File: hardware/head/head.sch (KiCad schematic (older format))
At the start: 51 parts, among them J1 DB9_Male, J10 Pump_Active, J2 Stats_Button, J3 Flush_Button, J4 Brew_Button, J5 Temp_Ok, J6 Display, J7 Load_Cell, J8 Rotary_Encoder, J9 Heater_Active, Q1 IRF540N, U1 Teensy4.0, U2 MAX757, U3 INA126, U4 INA126, U5 INA126

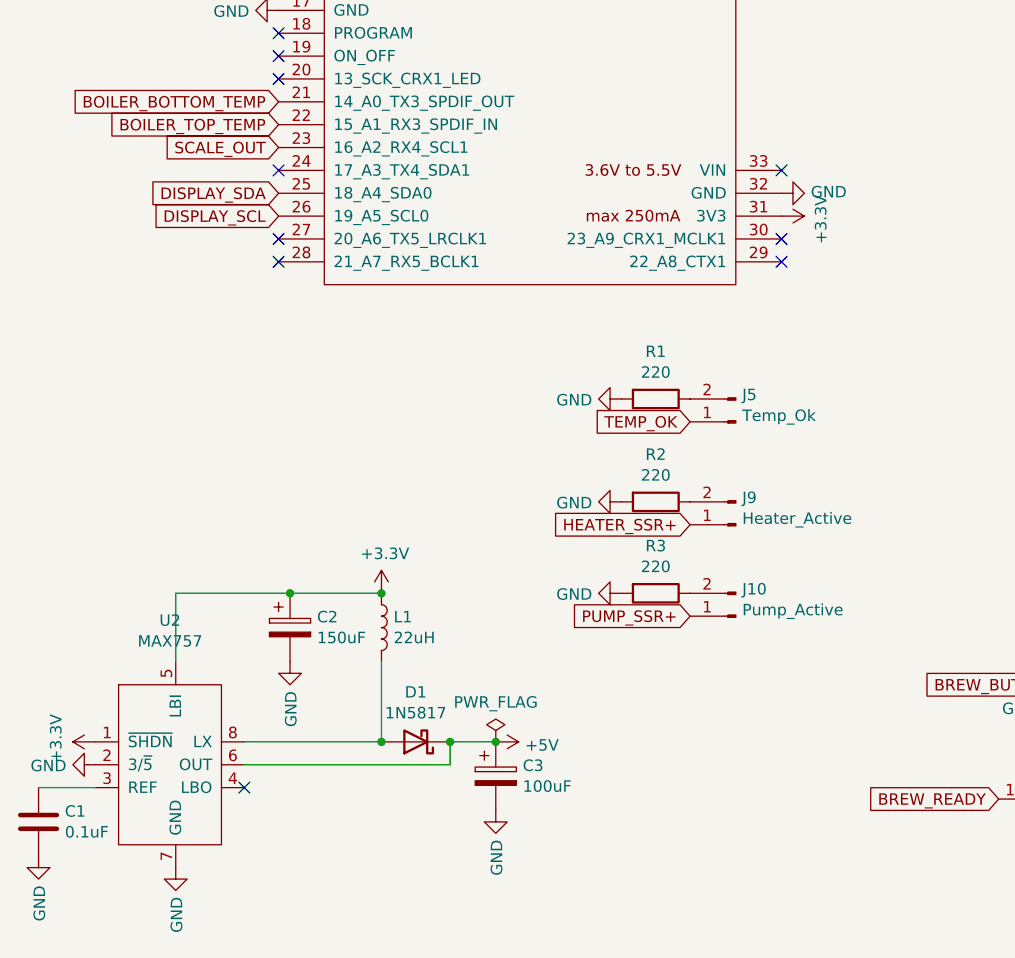
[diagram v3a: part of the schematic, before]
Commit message: Remove unnecessary boost converter
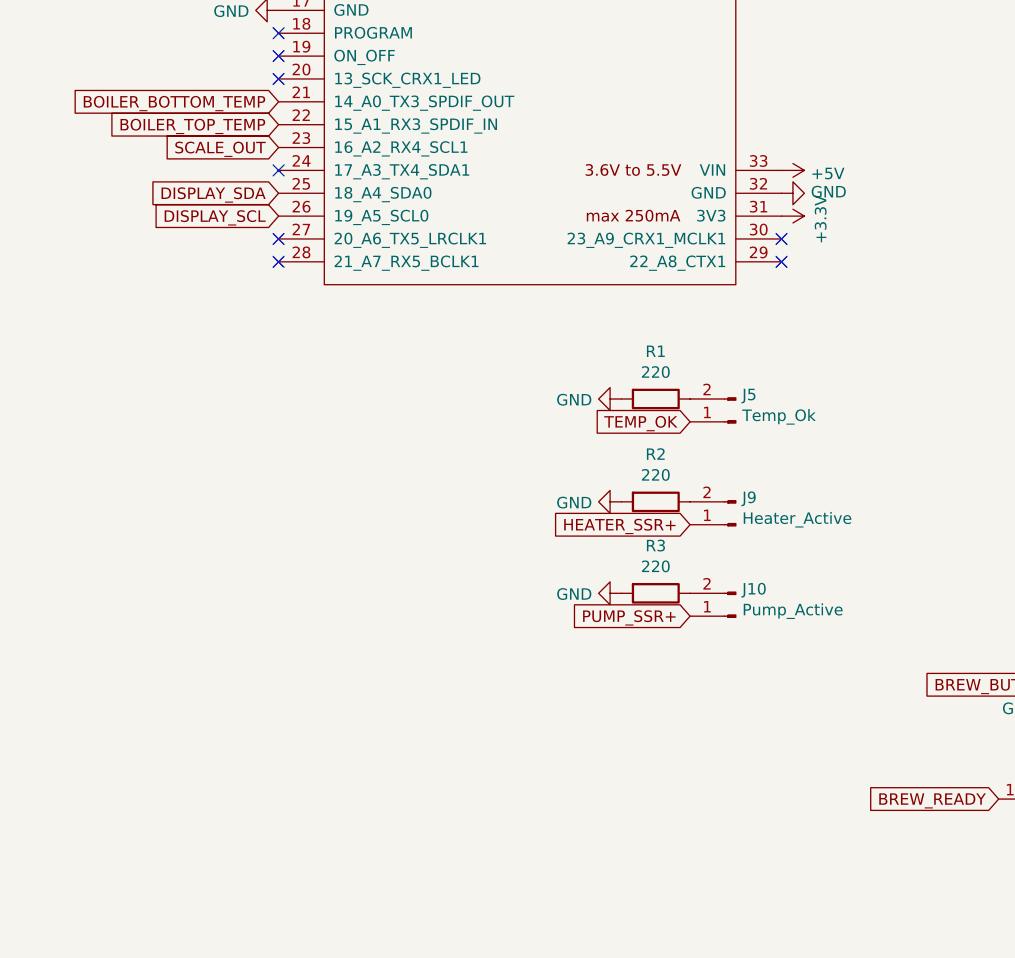
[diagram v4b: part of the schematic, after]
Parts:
- removed C1: 0.1uF, Capacitor_THT:C_Disc_D5.1mm_W3.2mm_P5.00mm, symbol Device:C
- removed C2: 150uF, Capacitor_THT:CP_Radial_D5.0mm_P2.00mm, symbol Device:CP
- removed C3: 100uF, Capacitor_THT:CP_Radial_D5.0mm_P2.00mm, symbol Device:CP
- removed D1: 1N5817, Diode_THT:D_DO-41_SOD81_P10.16mm_Horizontal, symbol Diode:1N5817
- removed L1: 22uH, Inductor_THT:L_Axial_L11.0mm_D4.5mm_P15.24mm_Horizontal_Fastron_MECC, symbol Device:L
- removed U2: MAX757, Package_DIP:DIP-8_W7.62mm, symbol boost_converter:MAX757
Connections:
- net +5V: now also U1.33 (VIN)
- no-connect marks 16 -> 14
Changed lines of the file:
@@
 NoConn ~ 1900 4600
 NoConn ~ 1900 4700
-NoConn ~ 4100 4300
 NoConn ~ 4100 4600
 NoConn ~ 4100 4700
@@
 SCALE_OUT
 $Comp
-L boost_converter:MAX757 U2
-U 1 1 6070BCF1
-P 1450 6900
-F 0 "U2" H 1425 7531 50  0000 C CNN
-F 1 "MAX757" H 1425 7440 50  0000 C CNN
-F 2 "Package_DIP:DIP-8_W7.62mm" H 1450 7600 50  0001 C CNN
-F 3 "" H 1450 7600 50  0001 C CNN
-	1    1450 6900
-	1    0    0    -1
-$EndComp
-$Comp
-L Device:C C1
-U 1 1 6070C612
-P 850 7150
-F 0 "C1" H 965 7196 50  0000 L CNN
-F 1 "0.1uF" H 965 7105 50  0000 L CNN
-F 2 "Capacitor_THT:C_Disc_D5.1mm_W3.2mm_P5.00mm" H 888 7000 50  0001 C CNN
-F 3 "~" H 850 7150 50  0001 C CNN
-	1    850  7150
-	1    0    0    -1
-$EndComp
-$Comp
-L Device:CP C2
-U 1 1 6070D658
-P 1950 6300
-F 0 "C2" H 2068 6346 50  0000 L CNN
-F 1 "150uF" H 2068 6255 50  0000 L CNN
-F 2 "Capacitor_THT:CP_Radial_D5.0mm_P2.00mm" H 1988 6150 50  0001 C CNN
-F 3 "~" H 1950 6300 50  0001 C CNN
-	1    1950 6300
-	1    0    0    -1
-$EndComp
-$Comp
-L Device:CP C3
-U 1 1 6070D8AB
-P 2850 6950
-F 0 "C3" H 2968 6996 50  0000 L CNN
-F 1 "100uF" H 2968 6905 50  0000 L CNN
-F 2 "Capacitor_THT:CP_Radial_D5.0mm_P2.00mm" H 2888 6800 50  0001 C CNN
-F 3 "~" H 2850 6950 50  0001 C CNN
-	1    2850 6950
-	1    0    0    -1
-$EndComp
-$Comp
-L power:GND #PWR010
-U 1 1 6070DB12
-P 1100 6900
-F 0 "#PWR010" H 1100 6650 50  0001 C CNN
-F 1 "GND" V 1105 6772 50  0000 R CNN
-F 2 "" H 1100 6900 50  0001 C CNN
-F 3 "" H 1100 6900 50  0001 C CNN
-	1    1100 6900
-	0    1    1    0
-$EndComp
-$Comp
-L power:+3.3V #PWR09
-U 1 1 6070EA45
-P 1100 6800
-F 0 "#PWR09" H 1100 6650 50  0001 C CNN
-F 1 "+3.3V" H 1115 6973 50  0000 C CNN
-F 2 "" H 1100 6800 50  0001 C CNN
-F 3 "" H 1100 6800 50  0001 C CNN
-	1    1100 6800
-	0    -1   -1   0
-$EndComp
-$Comp
-L power:GND #PWR06
-U 1 1 60710154
-P 850 7300
-F 0 "#PWR06" H 850 7050 50  0001 C CNN
-F 1 "GND" V 855 7172 50  0000 R CNN
-F 2 "" H 850 7300 50  0001 C CNN
-F 3 "" H 850 7300 50  0001 C CNN
-	1    850  7300
-	1    0    0    -1
-$EndComp
-Wire Wire Line
-	850  7000 1100 7000
-NoConn ~ 1750 7000
-$Comp
-L power:+3.3V #PWR013
-U 1 1 607179E9
-P 2350 6150
-F 0 "#PWR013" H 2350 6000 50  0001 C CNN
-F 1 "+3.3V" H 2365 6323 50  0000 C CNN
-F 2 "" H 2350 6150 50  0001 C CNN
-F 3 "" H 2350 6150 50  0001 C CNN
-	1    2350 6150
-	1    0    0    -1
-$EndComp
-$Comp
-L power:GND #PWR011
-U 1 1 6070E0B3
-P 1450 7350
-F 0 "#PWR011" H 1450 7100 50  0001 C CNN
-F 1 "GND" V 1455 7222 50  0000 R CNN
-F 2 "" H 1450 7350 50  0001 C CNN
-F 3 "" H 1450 7350 50  0001 C CNN
-	1    1450 7350
-	1    0    0    -1
-$EndComp
-$Comp
-L power:GND #PWR012
-U 1 1 6071A4A4
-P 1950 6450
-F 0 "#PWR012" H 1950 6200 50  0001 C CNN
-F 1 "GND" V 1955 6322 50  0000 R CNN
-F 2 "" H 1950 6450 50  0001 C CNN
-F 3 "" H 1950 6450 50  0001 C CNN
-	1    1950 6450
-	1    0    0    -1
-$EndComp
-$Comp
-L Device:L L1
-U 1 1 6071AEE1
-P 2350 6300
-F 0 "L1" H 2403 6346 50  0000 L CNN
-F 1 "22uH" H 2403 6255 50  0000 L CNN
-F 2 "Inductor_THT:L_Axial_L11.0mm_D4.5mm_P15.24mm_Horizontal_Fastron_MECC" H 2350 6300 50  0001 C CNN
-F 3 "~" H 2350 6300 50  0001 C CNN
-	1    2350 6300
-	1    0    0    -1
-$EndComp
-Wire Wire Line
-	1450 6450 1450 6150
-Wire Wire Line
-	1450 6150 1950 6150
-Wire Wire Line
-	1950 6150 2350 6150
-Connection ~ 1950 6150
-Connection ~ 2350 6150
-Wire Wire Line
-	1750 6800 2350 6800
-Wire Wire Line
-	2350 6800 2350 6450
-$Comp
-L Diode:1N5817 D1
-U 1 1 60722C26
-P 2500 6800
-F 0 "D1" H 2500 6583 50  0000 C CNN
-F 1 "1N5817" H 2500 6674 50  0000 C CNN
-F 2 "Diode_THT:D_DO-41_SOD81_P10.16mm_Horizontal" H 2500 6625 50  0001 C CNN
-F 3 "http://www.vishay.com/docs/88525/1n5817.pdf" H 2500 6800 50  0001 C CNN
-	1    2500 6800
-	-1   0    0    1
-$EndComp
-Connection ~ 2350 6800
-$Comp
-L power:GND #PWR015
-U 1 1 60724B14
-P 2850 7100
-F 0 "#PWR015" H 2850 6850 50  0001 C CNN
-F 1 "GND" V 2855 6972 50  0000 R CNN
-F 2 "" H 2850 7100 50  0001 C CNN
-F 3 "" H 2850 7100 50  0001 C CNN
-	1    2850 7100
-	1    0    0    -1
-$EndComp
-Wire Wire Line
-	2650 6800 2850 6800
-Wire Wire Line
-	2650 6800 2650 6900
-Wire Wire Line
-	2650 6900 1750 6900
-Connection ~ 2650 6800
-$Comp
-L power:+5V #PWR014
-U 1 1 60728197
-P 2850 6800
-F 0 "#PWR014" H 2850 6650 50  0001 C CNN
-F 1 "+5V" V 2865 6928 50  0000 L CNN
-F 2 "" H 2850 6800 50  0001 C CNN
-F 3 "" H 2850 6800 50  0001 C CNN
-	1    2850 6800
-	0    1    1    0
-$EndComp
-Connection ~ 2850 6800
-$Comp
 L power:+5V #PWR016
 U 1 1 6072C196
@@
 NoConn ~ 1900 3300
 NoConn ~ 1900 4300
-$Comp
-L power:PWR_FLAG #FLG0101
-U 1 1 6073ED1A
-P 2850 6800
-F 0 "#FLG0101" H 2850 6875 50  0001 C CNN
-F 1 "PWR_FLAG" H 2850 6973 50  0000 C CNN
-F 2 "" H 2850 6800 50  0001 C CNN
-F 3 "~" H 2850 6800 50  0001 C CNN
-	1    2850 6800
-	1    0    0    -1
-$EndComp
 Text GLabel 3700 5850 0    50   Input ~ 0
 HEATER_SSR+
@@
 	1    0    0    -1
 $EndComp
+$Comp
+L power:+5V #PWR?
+U 1 1 60BA5595
+P 4100 4300
+F 0 "#PWR?" H 4100 4150 50  0001 C CNN
+F 1 "+5V" V 4115 4428 50  0000 L CNN
+F 2 "" H 4100 4300 50  0001 C CNN
+F 3 "" H 4100 4300 50  0001 C CNN
+	1    4100 4300
+	0    1    1    0
+$EndComp
 $EndSCHEMATC
